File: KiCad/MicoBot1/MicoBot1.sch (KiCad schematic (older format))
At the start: 14 parts, among them J1 Conn_01x06_Male, J2 Screw_Terminal_01x02, J3 Conn_01x06_Male, SW1 SW_Push, SW2 SW_SPDT, U1 ATmega328P-PU, U2 L293D, U3 AMS1117-5.0, Y1 Crystal_Small

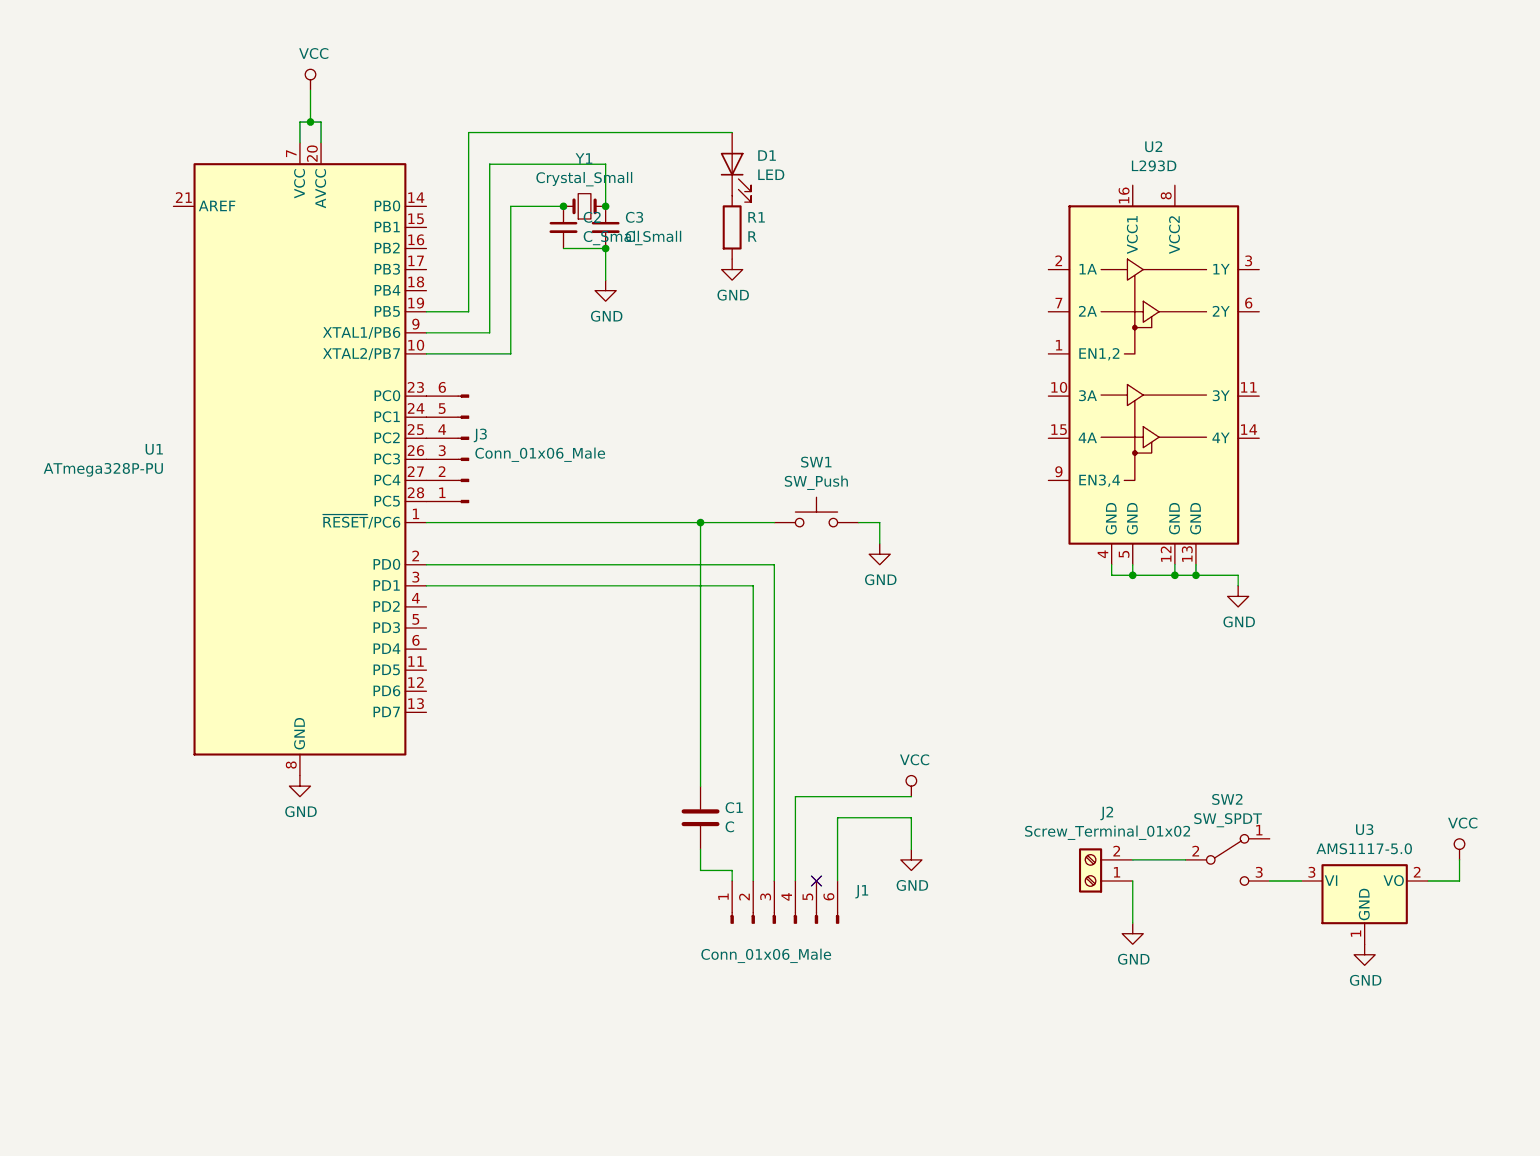
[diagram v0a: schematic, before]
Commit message: 
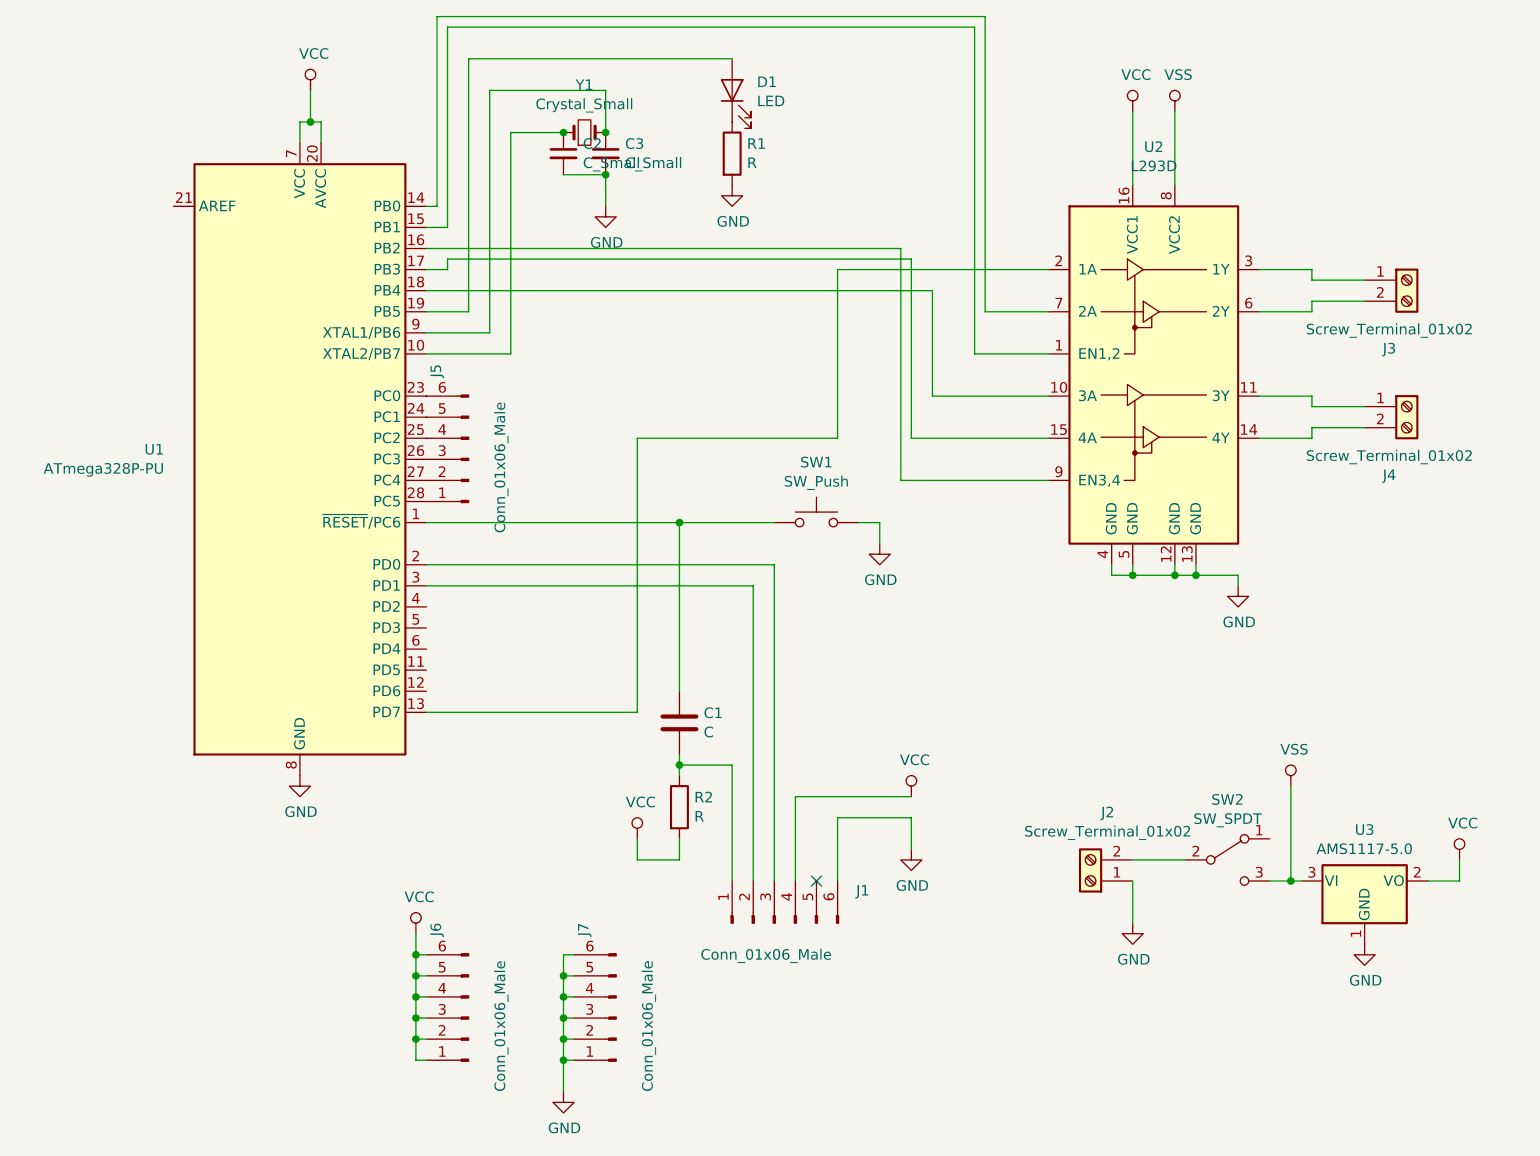
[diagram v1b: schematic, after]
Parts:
- removed J3: Conn_01x06_Male, Connector_PinHeader_2.54mm:PinHeader_1x06_P2.54mm_Vertical, symbol Connector:Conn_01x06_Male
- added J3, J4: Screw_Terminal_01x02, TerminalBlock_MetzConnect:TerminalBlock_MetzConnect_Type059_RT06302HBWC_1x02_P3.50mm_Horizontal, symbol Connector:Screw_Terminal_01x02
- added J5, J6, J7: Conn_01x06_Male, Connector_PinSocket_2.54mm:PinSocket_1x06_P2.54mm_Vertical, symbol Connector:Conn_01x06_Male
- added R2: R, Resistor_THT:R_Axial_DIN0204_L3.6mm_D1.6mm_P5.08mm_Horizontal, symbol Device:R
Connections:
- net GND: now also J7.1 (Pin_1), J7.2 (Pin_2), J7.3 (Pin_3), J7.4 (Pin_4), J7.5 (Pin_5), J7.6 (Pin_6)
- net VCC: now also U2.16 (VCC1), J6.1 (Pin_1), J6.2 (Pin_2), J6.3 (Pin_3), J6.4 (Pin_4), J6.5 (Pin_5), J6.6 (Pin_6), R2.2
- net at U1.13 (PD7): now also U2.2 (1A)
- net at U1.14 (PB0): now also U2.7 (2A)
- net at U1.15 (PB1): now also U2.1 (EN1,2)
- net at U1.16 (PB2): now also U2.9 (EN3,4)
- net at U1.17 (PB3): now also U2.15 (4A)
- net at U1.18 (PB4): now also U2.10 (3A)
- net at U1.23 (PC0): now also J5.6 (Pin_6)
- net at U1.24 (PC1): now also J5.5 (Pin_5)
- net at U1.25 (PC2): now also J5.4 (Pin_4)
- net at U1.26 (PC3): now also J5.3 (Pin_3)
- net at U1.27 (PC4): now also J5.2 (Pin_2)
- net at U1.28 (PC5): now also J5.1 (Pin_1)
- net at C1.2, J1.1 (Pin_1): now also R2.1
- net VSS: now reaches SW2.3 (C), U3.3 (VI)
- net VSS: now also U2.8 (VCC2)
- net at U2.11 (3Y): now also J4.1 (Pin_1)
- net at U2.14 (4Y): now also J4.2 (Pin_2)
- net at U2.3 (1Y): now also J3.1 (Pin_1)
- net at U2.6 (2Y): now also J3.2 (Pin_2)
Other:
- moved on the sheet: C1, C2, C3, D1, R1, Y1

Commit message: 
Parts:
- Y1: footprint Crystal:Crystal_HC18-U_Vertical -> Crystal:Crystal_HC49-4H_Vertical
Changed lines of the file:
@@
 F 0 "Y1" H 4900 1625 50  0000 C CNN
 F 1 "Crystal_Small" H 4900 1534 50  0000 C CNN
-F 2 "Crystal:Crystal_HC18-U_Vertical" H 4900 1400 50  0001 C CNN
+F 2 "Crystal:Crystal_HC49-4H_Vertical" H 4900 1400 50  0001 C CNN
 F 3 "~" H 4900 1400 50  0001 C CNN
 	1    4900 1400

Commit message: 
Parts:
- C2, C3: value C_Small -> C
- J1: value Conn_01x06_Male -> Prog
- J2: value Screw_Terminal_01x02 -> Bat
- J3: value Screw_Terminal_01x02 -> Motor2
- J4: value Screw_Terminal_01x02 -> Motor1
- J5: value Conn_01x06_Male -> Datos
- J6: value Conn_01x06_Male -> Vcc
- J7: value Conn_01x06_Male -> Gnd
- SW1: value SW_Push -> Rst
- SW2: value SW_SPDT -> On
- Y1: value Crystal_Small -> Crystal
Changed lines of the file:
@@
 P 5800 5150
 F 0 "J1" V 5954 4762 50  0000 R CNN
-F 1 "Conn_01x06_Male" V 5650 5500 50  0000 R CNN
+F 1 "Prog" V 5700 5250 50  0000 R CNN
 F 2 "Connector_PinHeader_2.54mm:PinHeader_1x06_P2.54mm_Vertical" H 5800 5150 50  0001 C CNN
 F 3 "~" H 5800 5150 50  0001 C CNN
@@
 P 6000 3250
 F 0 "SW1" H 6000 3535 50  0000 C CNN
-F 1 "SW_Push" H 6000 3444 50  0000 C CNN
+F 1 "Rst" H 6000 3444 50  0000 C CNN
 F 2 "MiLib:Pulsador_Cuadrado_6" H 6000 3450 50  0001 C CNN
 F 3 "~" H 6000 3450 50  0001 C CNN
@@
 P 7300 4950
 F 0 "J2" H 7218 4625 50  0000 C CNN
-F 1 "Screw_Terminal_01x02" H 7218 4716 50  0000 C CNN
+F 1 "Bat" H 7218 4716 50  0000 C CNN
 F 2 "TerminalBlock_MetzConnect:TerminalBlock_MetzConnect_Type059_RT06302HBWC_1x02_P3.50mm_Horizontal" H 7300 4950 50  0001 C CNN
 F 3 "~" H 7300 4950 50  0001 C CNN
@@
 P 7950 4850
 F 0 "SW2" H 7950 5135 50  0000 C CNN
-F 1 "SW_SPDT" H 7950 5044 50  0000 C CNN
+F 1 "On" H 7950 5044 50  0000 C CNN
 F 2 "MiLib:EG1218" H 7950 4850 50  0001 C CNN
 F 3 "~" H 7950 4850 50  0001 C CNN
@@
 P 4900 1400
 F 0 "Y1" H 4900 1625 50  0000 C CNN
-F 1 "Crystal_Small" H 4900 1534 50  0000 C CNN
+F 1 "Crystal" H 4900 1534 50  0000 C CNN
 F 2 "Crystal:Crystal_HC49-4H_Vertical" H 4900 1400 50  0001 C CNN
 F 3 "~" H 4900 1400 50  0001 C CNN
@@
 P 4800 1500
 F 0 "C2" H 4892 1546 50  0000 L CNN
-F 1 "C_Small" H 4892 1455 50  0000 L CNN
+F 1 "C" H 4892 1455 50  0000 L CNN
 F 2 "Capacitor_THT:C_Disc_D4.3mm_W1.9mm_P5.00mm" H 4800 1500 50  0001 C CNN
 F 3 "~" H 4800 1500 50  0001 C CNN
@@
 P 5000 1500
 F 0 "C3" H 5092 1546 50  0000 L CNN
-F 1 "C_Small" H 5092 1455 50  0000 L CNN
+F 1 "C" H 5092 1455 50  0000 L CNN
 F 2 "Capacitor_THT:C_Disc_D4.3mm_W1.9mm_P5.00mm" H 5000 1500 50  0001 C CNN
 F 3 "~" H 5000 1500 50  0001 C CNN
@@
 P 8800 2100
 F 0 "J3" H 8718 1775 50  0000 C CNN
-F 1 "Screw_Terminal_01x02" H 8718 1866 50  0000 C CNN
+F 1 "Motor2" H 8718 1866 50  0000 C CNN
 F 2 "TerminalBlock_MetzConnect:TerminalBlock_MetzConnect_Type059_RT06302HBWC_1x02_P3.50mm_Horizontal" H 8800 2100 50  0001 C CNN
 F 3 "~" H 8800 2100 50  0001 C CNN
@@
 P 8800 2700
 F 0 "J4" H 8718 2375 50  0000 C CNN
-F 1 "Screw_Terminal_01x02" H 8718 2466 50  0000 C CNN
+F 1 "Motor1" H 8718 2466 50  0000 C CNN
 F 2 "TerminalBlock_MetzConnect:TerminalBlock_MetzConnect_Type059_RT06302HBWC_1x02_P3.50mm_Horizontal" H 8800 2700 50  0001 C CNN
 F 3 "~" H 8800 2700 50  0001 C CNN
@@
 P 4350 2950
 F 0 "J5" V 4504 2562 50  0000 R CNN
-F 1 "Conn_01x06_Male" V 4200 3300 50  0000 R CNN
+F 1 "Datos" V 4250 3000 50  0000 R CNN
 F 2 "Connector_PinSocket_2.54mm:PinSocket_1x06_P2.54mm_Vertical" H 4350 2950 50  0001 C CNN
 F 3 "~" H 4350 2950 50  0001 C CNN
@@
 P 4350 5600
 F 0 "J6" V 4504 5212 50  0000 R CNN
-F 1 "Conn_01x06_Male" V 4200 5950 50  0000 R CNN
+F 1 "Vcc" V 4250 5600 50  0000 R CNN
 F 2 "Connector_PinSocket_2.54mm:PinSocket_1x06_P2.54mm_Vertical" H 4350 5600 50  0001 C CNN
 F 3 "~" H 4350 5600 50  0001 C CNN
@@
 P 5050 5600
 F 0 "J7" V 5204 5212 50  0000 R CNN
-F 1 "Conn_01x06_Male" V 4900 5950 50  0000 R CNN
+F 1 "Gnd" V 4950 5650 50  0000 R CNN
 F 2 "Connector_PinSocket_2.54mm:PinSocket_1x06_P2.54mm_Vertical" H 5050 5600 50  0001 C CNN
 F 3 "~" H 5050 5600 50  0001 C CNN

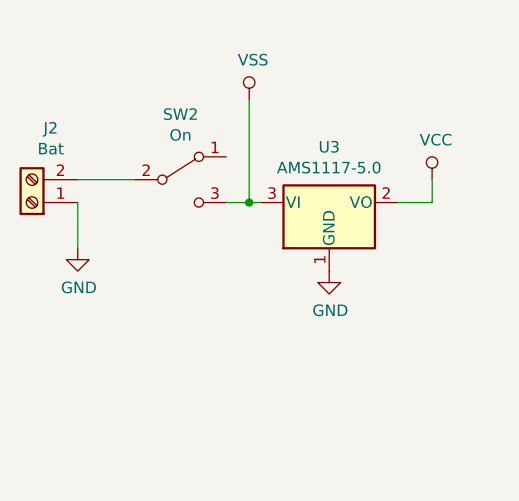
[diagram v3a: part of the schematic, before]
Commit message: 
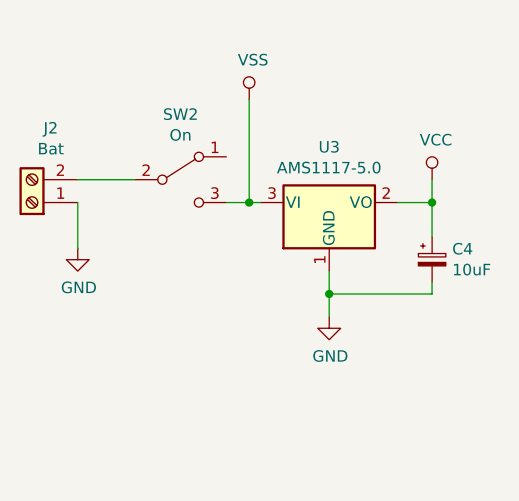
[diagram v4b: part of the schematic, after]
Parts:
- added C4: 10uF, Capacitor_THT:C_Radial_D5.0mm_H5.0mm_P2.00mm, symbol Device:CP_Small
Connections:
- net GND: now also C4.2
- net VCC: now also C4.1
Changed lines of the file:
@@
 L power:GND #PWR0101
 U 1 1 5CB7D70C
-P 8600 5250
-F 0 "#PWR0101" H 8600 5000 50  0001 C CNN
-F 1 "GND" H 8605 5077 50  0000 C CNN
-F 2 "" H 8600 5250 50  0001 C CNN
-F 3 "" H 8600 5250 50  0001 C CNN
-	1    8600 5250
+P 8600 5450
+F 0 "#PWR0101" H 8600 5200 50  0001 C CNN
+F 1 "GND" H 8605 5277 50  0000 C CNN
+F 2 "" H 8600 5450 50  0001 C CNN
+F 3 "" H 8600 5450 50  0001 C CNN
+	1    8600 5450
 	1    0    0    -1
 $EndComp
@@
 Wire Wire Line
 	6550 2150 6550 2650
+Wire Wire Line
+	8600 5250 8600 5350
+$Comp
+L Device:CP_Small C4
+U 1 1 5D4DC0CB
+P 9050 5200
+F 0 "C4" H 9138 5246 50  0000 L CNN
+F 1 "10uF" H 9138 5155 50  0000 L CNN
+F 2 "Capacitor_THT:C_Radial_D5.0mm_H5.0mm_P2.00mm" H 9050 5200 50  0001 C CNN
+F 3 "~" H 9050 5200 50  0001 C CNN
+	1    9050 5200
+	1    0    0    -1
+$EndComp
+Wire Wire Line
+	9050 4950 9050 5100
+Connection ~ 9050 4950
+Wire Wire Line
+	9050 5300 9050 5350
+Wire Wire Line
+	9050 5350 8600 5350
+Connection ~ 8600 5350
+Wire Wire Line
+	8600 5350 8600 5450
 $EndSCHEMATC

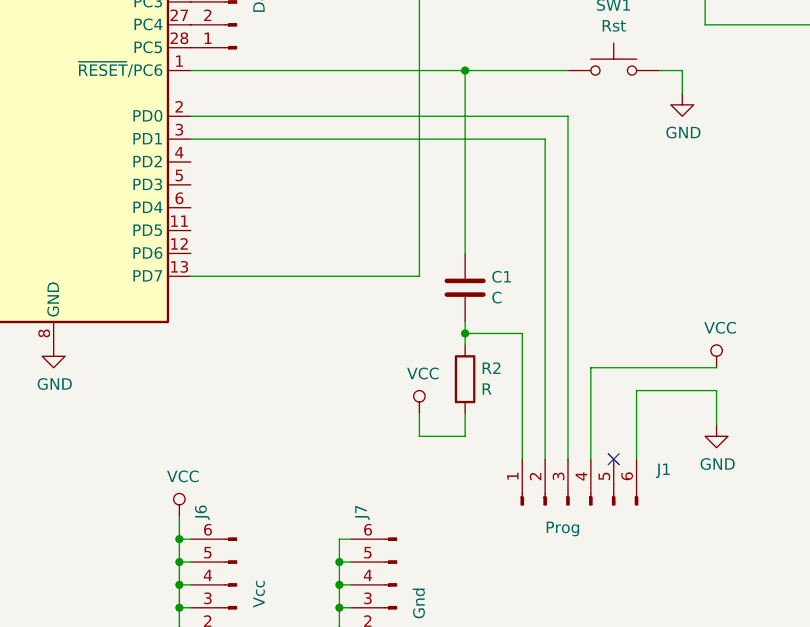
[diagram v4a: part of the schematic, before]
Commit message: 
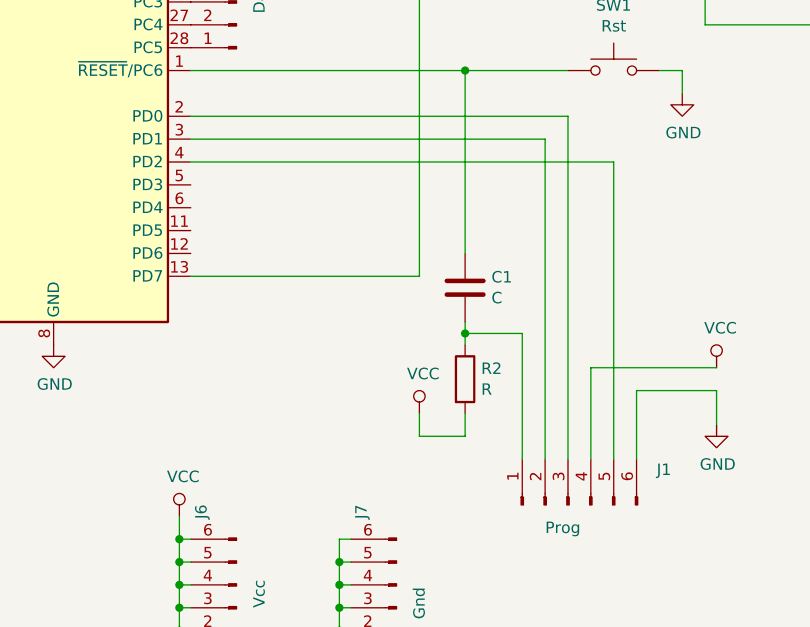
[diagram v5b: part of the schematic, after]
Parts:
- J2, J3, J4: footprint TerminalBlock_MetzConnect:TerminalBlock_MetzConnect_Type059_RT06302HBWC_1x02_P3.50mm_Horizontal -> TerminalBlock_Phoenix:TerminalBlock_Phoenix_PT-1,5-2-3.5-H_1x02_P3.50mm_Horizontal
- J5, J6, J7: footprint Connector_PinSocket_2.54mm:PinSocket_1x06_P2.54mm_Vertical -> Connector_PinHeader_2.54mm:PinHeader_1x06_P2.54mm_Vertical
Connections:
- net at U1.4 (PD2): now also J1.5 (Pin_5)
- no-connect marks 1 -> 0
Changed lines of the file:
@@
 Wire Wire Line
 	6450 4650 6450 4800
-NoConn ~ 6000 4950
 Wire Wire Line
 	5900 4950 5900 4550
@@
 F 0 "J2" H 7218 4625 50  0000 C CNN
 F 1 "Bat" H 7218 4716 50  0000 C CNN
-F 2 "TerminalBlock_MetzConnect:TerminalBlock_MetzConnect_Type059_RT06302HBWC_1x02_P3.50mm_Horizontal" H 7300 4950 50  0001 C CNN
+F 2 "TerminalBlock_Phoenix:TerminalBlock_Phoenix_PT-1,5-2-3.5-H_1x02_P3.50mm_Horizontal" H 7300 4950 50  0001 C CNN
 F 3 "~" H 7300 4950 50  0001 C CNN
 	1    7300 4950
@@
 F 0 "J3" H 8718 1775 50  0000 C CNN
 F 1 "Motor2" H 8718 1866 50  0000 C CNN
-F 2 "TerminalBlock_MetzConnect:TerminalBlock_MetzConnect_Type059_RT06302HBWC_1x02_P3.50mm_Horizontal" H 8800 2100 50  0001 C CNN
+F 2 "TerminalBlock_Phoenix:TerminalBlock_Phoenix_PT-1,5-2-3.5-H_1x02_P3.50mm_Horizontal" H 8800 2100 50  0001 C CNN
 F 3 "~" H 8800 2100 50  0001 C CNN
 	1    8800 2100
@@
 F 0 "J4" H 8718 2375 50  0000 C CNN
 F 1 "Motor1" H 8718 2466 50  0000 C CNN
-F 2 "TerminalBlock_MetzConnect:TerminalBlock_MetzConnect_Type059_RT06302HBWC_1x02_P3.50mm_Horizontal" H 8800 2700 50  0001 C CNN
+F 2 "TerminalBlock_Phoenix:TerminalBlock_Phoenix_PT-1,5-2-3.5-H_1x02_P3.50mm_Horizontal" H 8800 2700 50  0001 C CNN
 F 3 "~" H 8800 2700 50  0001 C CNN
 	1    8800 2700
@@
 F 0 "J5" V 4504 2562 50  0000 R CNN
 F 1 "Datos" V 4250 3000 50  0000 R CNN
-F 2 "Connector_PinSocket_2.54mm:PinSocket_1x06_P2.54mm_Vertical" H 4350 2950 50  0001 C CNN
+F 2 "Connector_PinHeader_2.54mm:PinHeader_1x06_P2.54mm_Vertical" H 4350 2950 50  0001 C CNN
 F 3 "~" H 4350 2950 50  0001 C CNN
 	1    4350 2950
@@
 F 0 "J6" V 4504 5212 50  0000 R CNN
 F 1 "Vcc" V 4250 5600 50  0000 R CNN
-F 2 "Connector_PinSocket_2.54mm:PinSocket_1x06_P2.54mm_Vertical" H 4350 5600 50  0001 C CNN
+F 2 "Connector_PinHeader_2.54mm:PinHeader_1x06_P2.54mm_Vertical" H 4350 5600 50  0001 C CNN
 F 3 "~" H 4350 5600 50  0001 C CNN
 	1    4350 5600
@@
 F 0 "J7" V 5204 5212 50  0000 R CNN
 F 1 "Gnd" V 4950 5650 50  0000 R CNN
-F 2 "Connector_PinSocket_2.54mm:PinSocket_1x06_P2.54mm_Vertical" H 5050 5600 50  0001 C CNN
+F 2 "Connector_PinHeader_2.54mm:PinHeader_1x06_P2.54mm_Vertical" H 5050 5600 50  0001 C CNN
 F 3 "~" H 5050 5600 50  0001 C CNN
 	1    5050 5600
@@
 Wire Wire Line
 	8600 5350 8600 5450
+Wire Wire Line
+	4150 3650 6000 3650
+Wire Wire Line
+	6000 3650 6000 4950
 $EndSCHEMATC
